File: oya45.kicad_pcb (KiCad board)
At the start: 2 copper layers, 94 parts, among them U1 Elite-C

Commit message: diodes lined up
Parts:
- moved U1 295.5 mm to (213.9, -7.87)
- moved D25 192.2 mm to (-50.2, 37.5), turned to 90 degrees
- moved D22 187.4 mm to (-58.3, 37.5), turned to 90 degrees
- moved D19 182.8 mm to (-62.4, 37.5), turned to 90 degrees
- moved D18 180.3 mm to (-64.4, 37.5), turned to 90 degrees
- moved D17 177.8 mm to (-66.4, 37.5), turned to 90 degrees
- moved D16 175.3 mm to (-68.5, 37.5), turned to 90 degrees
- moved D15 172.8 mm to (-70.5, 37.5), turned to 90 degrees
- moved D9 159.6 mm to (-82.7, 37.5), turned to 90 degrees
- moved D8 157.3 mm to (-84.7, 37.5), turned to 90 degrees
- moved D7 155.0 mm to (-86.7, 37.5), turned to 90 degrees
- moved D44 151.2 mm to (-11.6, 37.5), turned to 90 degrees
- moved D2 146.4 mm to (-96.9, 37.5), turned to 90 degrees
- moved D40 142.8 mm to (-19.7, 37.5), turned to 90 degrees
- moved D39 140.5 mm to (-21.7, 37.5), turned to 90 degrees
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
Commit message: less pads
made a basic pcb instead of complex to make it cheaper
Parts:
- moved D23 252.8 mm to (198.5, 42.5)
- moved D21 252.8 mm to (196.5, 42.5)
- moved D1 252.7 mm to (153.8, 42.5)
- moved D12 252.7 mm to (176.1, 42.5)
- moved D17 252.7 mm to (186.3, 42.5)
- moved D20 252.7 mm to (192.4, 42.5)
- moved D4 252.7 mm to (159.9, 42.5)
- moved D9 252.7 mm to (170.0, 42.5)
- moved D11 252.7 mm to (174.1, 42.5)
- moved D13 252.7 mm to (178.1, 42.5)
- moved D14 252.7 mm to (180.2, 42.5)
- moved D16 252.7 mm to (184.2, 42.5)
- moved D19 252.7 mm to (190.3, 42.5)
- moved D22 252.7 mm to (194.4, 42.5)
- moved D3 252.7 mm to (157.8, 42.5)
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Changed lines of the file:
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@@
   )
   (module Keebio-Parts:Diode-Hybrid-Back (layer B.Cu)
-    (at -9.525 37.465 90)
+    (at 196.50075 32.54375 90)
     (attr smd)
     (fp_text reference D45 (at -0.0254 -1.4 90) (layer F.SilkS)
@@
   )
   (module Keebio-Parts:Diode-Hybrid-Back (layer B.Cu)
-    (at -11.557 37.465 90)
+    (at 194.46875 32.54375 90)
     (attr smd)
     (fp_text reference D44 (at -0.0254 -1.4 90) (layer F.SilkS)
@@
   )
   (module Keebio-Parts:Diode-Hybrid-Back (layer B.Cu)
-    (at -13.589 37.465 90)
+    (at 192.43675 32.54375 90)
     (attr smd)
     (fp_text reference D43 (at -0.0254 -1.4 90) (layer F.SilkS)
@@
   )
   (module Keebio-Parts:Diode-Hybrid-Back (layer B.Cu)
-    (at -15.621 37.465 90)
+    (at 190.40475 32.54375 90)
     (attr smd)
     (fp_text reference D42 (at -0.0254 -1.4 90) (layer F.SilkS)
@@
   )
   (module Keebio-Parts:Diode-Hybrid-Back (layer B.Cu)
-    (at -17.653 37.465 90)
+    (at 188.37275 32.54375 90)
     (attr smd)
     (fp_text reference D41 (at -0.0254 -1.4 90) (layer F.SilkS)
@@
   )
   (module Keebio-Parts:Diode-Hybrid-Back (layer B.Cu)
-    (at -19.685 37.465 90)
+    (at 186.34075 32.54375 90)
     (attr smd)
     (fp_text reference D40 (at -0.0254 -1.4 90) (layer F.SilkS)
@@
   )
   (module Keebio-Parts:Diode-Hybrid-Back (layer B.Cu)
-    (at -21.717 37.465 90)
+    (at 184.30875 32.54375 90)
     (attr smd)
     (fp_text reference D39 (at -0.0254 -1.4 90) (layer F.SilkS)
@@
   )
   (module Keebio-Parts:Diode-Hybrid-Back (layer B.Cu)
-    (at -23.749 37.465 90)
+    (at 182.27675 32.54375 90)
     (attr smd)
     (fp_text reference D38 (at -0.0254 -1.4 90) (layer F.SilkS)
@@
   )
   (module Keebio-Parts:Diode-Hybrid-Back (layer B.Cu)
-    (at -25.781 37.465 90)
+    (at 180.24475 32.54375 90)
     (attr smd)
     (fp_text reference D37 (at -0.0254 -1.4 90) (layer F.SilkS)
@@
   )
   (module Keebio-Parts:Diode-Hybrid-Back (layer B.Cu)
-    (at -27.813 37.465 90)
+    (at 178.21275 32.54375 90)
     (attr smd)
     (fp_text reference D36 (at -0.0254 -1.4 90) (layer F.SilkS)
@@
   )
   (module Keebio-Parts:Diode-Hybrid-Back (layer B.Cu)
-    (at -29.845 37.465 90)
+    (at 176.18075 32.54375 90)
     (attr smd)
     (fp_text reference D35 (at -0.0254 -1.4 90) (layer F.SilkS)
@@
   )
   (module Keebio-Parts:Diode-Hybrid-Back (layer B.Cu)
-    (at -31.877 37.465 90)
+    (at 174.14875 32.54375 90)
     (attr smd)
     (fp_text reference D34 (at -0.0254 -1.4 90) (layer F.SilkS)
@@
   )
   (module Keebio-Parts:Diode-Hybrid-Back (layer B.Cu)
-    (at -33.909 37.465 90)
+    (at 172.11675 32.54375 90)
     (attr smd)
     (fp_text reference D33 (at -0.0254 -1.4 90) (layer F.SilkS)
@@
   )
   (module Keebio-Parts:Diode-Hybrid-Back (layer B.Cu)
-    (at -35.941 37.465 90)
+    (at 170.08475 32.54375 90)
     (attr smd)
     (fp_text reference D32 (at -0.0254 -1.4 90) (layer F.SilkS)
@@
   )
   (module Keebio-Parts:Diode-Hybrid-Back (layer B.Cu)
-    (at -37.973 37.465 90)
+    (at 168.05275 32.54375 90)
     (attr smd)
     (fp_text reference D31 (at -0.0254 -1.4 90) (layer F.SilkS)
@@
   )
   (module Keebio-Parts:Diode-Hybrid-Back (layer B.Cu)
-    (at -40.005 37.465 90)
+    (at 166.02075 32.54375 90)
     (attr smd)
     (fp_text reference D30 (at -0.0254 -1.4 90) (layer F.SilkS)
@@
   )
   (module Keebio-Parts:Diode-Hybrid-Back (layer B.Cu)
-    (at -42.037 37.465 90)
+    (at 163.98875 32.54375 90)
     (attr smd)
     (fp_text reference D29 (at -0.0254 -1.4 90) (layer F.SilkS)
@@
   )
   (module Keebio-Parts:Diode-Hybrid-Back (layer B.Cu)
-    (at -44.069 37.465 90)
+    (at 161.95675 32.54375 90)
     (attr smd)
     (fp_text reference D28 (at -0.0254 -1.4 90) (layer F.SilkS)
@@
   )
   (module Keebio-Parts:Diode-Hybrid-Back (layer B.Cu)
-    (at -46.101 37.465 90)
+    (at 159.92475 32.54375 90)
     (attr smd)
     (fp_text reference D27 (at -0.0254 -1.4 90) (layer F.SilkS)
@@
   )
   (module Keebio-Parts:Diode-Hybrid-Back (layer B.Cu)
-    (at -48.133 37.465 90)
+    (at 157.89275 32.54375 90)
     (attr smd)
     (fp_text reference D26 (at -0.0254 -1.4 90) (layer F.SilkS)
@@
   )
   (module Keebio-Parts:Diode-Hybrid-Back (layer B.Cu)
-    (at -50.165 37.465 90)
+    (at 155.86075 32.54375 90)
     (attr smd)
     (fp_text reference D25 (at -0.0254 -1.4 90) (layer F.SilkS)
@@
   )
   (module Keebio-Parts:Diode-Hybrid-Back (layer B.Cu)
-    (at -52.197 37.465 90)
+    (at 153.82875 32.54375 90)
     (attr smd)
     (fp_text reference D24 (at -0.0254 -1.4 90) (layer F.SilkS)
@@
   )
   (module Keebio-Parts:Diode-Hybrid-Back (layer B.Cu)
-    (at -54.229 37.465 90)
+    (at 198.501 42.545 90)
     (attr smd)
     (fp_text reference D23 (at -0.0254 -1.4 90) (layer F.SilkS)
@@
   )
   (module Keebio-Parts:Diode-Hybrid-Back (layer B.Cu)
-    (at -58.293 37.465 90)
+    (at 194.40525 42.545 90)
     (attr smd)
     (fp_text reference D22 (at -0.0254 -1.4 90) (layer F.SilkS)
@@
   )
   (module Keebio-Parts:Diode-Hybrid-Back (layer B.Cu)
-    (at -56.261 37.465 90)
+    (at 196.469 42.545 90)
     (attr smd)
     (fp_text reference D21 (at -0.0254 -1.4 90) (layer F.SilkS)
@@
   )
   (module Keebio-Parts:Diode-Hybrid-Back (layer B.Cu)
-    (at -60.325 37.465 90)
+    (at 192.37325 42.545 90)
     (attr smd)
     (fp_text reference D20 (at -0.0254 -1.4 90) (layer F.SilkS)
@@
   )
   (module Keebio-Parts:Diode-Hybrid-Back (layer B.Cu)
-    (at -62.357 37.465 90)
+    (at 190.34125 42.545 90)
     (attr smd)
     (fp_text reference D19 (at -0.0254 -1.4 90) (layer F.SilkS)
@@
   )
   (module Keebio-Parts:Diode-Hybrid-Back (layer B.Cu)
-    (at -64.389 37.465 90)
+    (at 188.30925 42.545 90)
     (attr smd)
     (fp_text reference D18 (at -0.0254 -1.4 90) (layer F.SilkS)
@@
   )
   (module Keebio-Parts:Diode-Hybrid-Back (layer B.Cu)
-    (at -66.421 37.465 90)
+    (at 186.27725 42.545 90)
     (attr smd)
     (fp_text reference D17 (at -0.0254 -1.4 90) (layer F.SilkS)
@@
   )
   (module Keebio-Parts:Diode-Hybrid-Back (layer B.Cu)
-    (at -68.453 37.465 90)
+    (at 184.24525 42.545 90)
     (attr smd)
     (fp_text reference D16 (at -0.0254 -1.4 90) (layer F.SilkS)
@@
   )
   (module Keebio-Parts:Diode-Hybrid-Back (layer B.Cu)
-    (at -70.485 37.465 90)
+    (at 182.21325 42.545 90)
     (attr smd)
     (fp_text reference D15 (at -0.0254 -1.4 90) (layer F.SilkS)
@@
   )
   (module Keebio-Parts:Diode-Hybrid-Back (layer B.Cu)
-    (at -72.517 37.465 90)
+    (at 180.18125 42.545 90)
     (attr smd)
     (fp_text reference D14 (at -0.0254 -1.4 90) (layer F.SilkS)
@@
   )
   (module Keebio-Parts:Diode-Hybrid-Back (layer B.Cu)
-    (at -74.549 37.465 90)
+    (at 178.14925 42.545 90)
     (attr smd)
     (fp_text reference D13 (at -0.0254 -1.4 90) (layer F.SilkS)
@@
   )
   (module Keebio-Parts:Diode-Hybrid-Back (layer B.Cu)
-    (at -76.581 37.465 90)
+    (at 176.11725 42.545 90)
     (attr smd)
     (fp_text reference D12 (at -0.0254 -1.4 90) (layer F.SilkS)
@@
   )
   (module Keebio-Parts:Diode-Hybrid-Back (layer B.Cu)
-    (at -78.613 37.465 90)
+    (at 174.08525 42.545 90)
     (attr smd)
     (fp_text reference D11 (at -0.0254 -1.4 90) (layer F.SilkS)
@@
   )
   (module Keebio-Parts:Diode-Hybrid-Back (layer B.Cu)
-    (at -80.645 37.465 90)
+    (at 172.05325 42.545 90)
     (attr smd)
     (fp_text reference D10 (at -0.0254 -1.4 90) (layer F.SilkS)
@@
   )
   (module Keebio-Parts:Diode-Hybrid-Back (layer B.Cu)
-    (at -82.677 37.465 90)
+    (at 170.02125 42.545 90)
     (attr smd)
     (fp_text reference D9 (at -0.0254 -1.4 90) (layer F.SilkS)
@@
   )
   (module Keebio-Parts:Diode-Hybrid-Back (layer B.Cu)
-    (at -84.709 37.465 90)
+    (at 167.98925 42.545 90)
     (attr smd)
     (fp_text reference D8 (at -0.0254 -1.4 90) (layer F.SilkS)
@@
   )
   (module Keebio-Parts:Diode-Hybrid-Back (layer B.Cu)
-    (at -86.741 37.465 90)
+    (at 165.95725 42.545 90)
     (attr smd)
     (fp_text reference D7 (at -0.0254 -1.4 90) (layer F.SilkS)
@@
   )
   (module Keebio-Parts:Diode-Hybrid-Back (layer B.Cu)
-    (at -88.773 37.465 90)
+    (at 163.92525 42.545 90)
     (attr smd)
     (fp_text reference D6 (at -0.0254 -1.4 90) (layer F.SilkS)
@@
   )
   (module Keebio-Parts:Diode-Hybrid-Back (layer B.Cu)
-    (at -90.805 37.465 90)
+    (at 161.89325 42.545 90)
     (attr smd)
     (fp_text reference D5 (at -0.0254 -1.4 90) (layer F.SilkS)
@@
   )
   (module Keebio-Parts:Diode-Hybrid-Back (layer B.Cu)
-    (at -92.837 37.465 90)
+    (at 159.86125 42.545 90)
     (attr smd)
     (fp_text reference D4 (at -0.0254 -1.4 90) (layer F.SilkS)
@@
   )
   (module Keebio-Parts:Diode-Hybrid-Back (layer B.Cu)
-    (at -94.869 37.465 90)
+    (at 157.82925 42.545 90)
     (attr smd)
     (fp_text reference D3 (at -0.0254 -1.4 90) (layer F.SilkS)
@@
   )
   (module Keebio-Parts:Diode-Hybrid-Back (layer B.Cu)
-    (at -96.901 37.465 90)
+    (at 155.79725 42.545 90)
     (attr smd)
     (fp_text reference D2 (at -0.0254 -1.4 90) (layer F.SilkS)
@@
   )
   (module Keebio-Parts:Diode-Hybrid-Back (layer B.Cu)
-    (at -98.933 37.465 90)
+    (at 153.76525 42.545 90)
     (attr smd)
     (fp_text reference D1 (at -0.0254 -1.4 90) (layer F.SilkS)

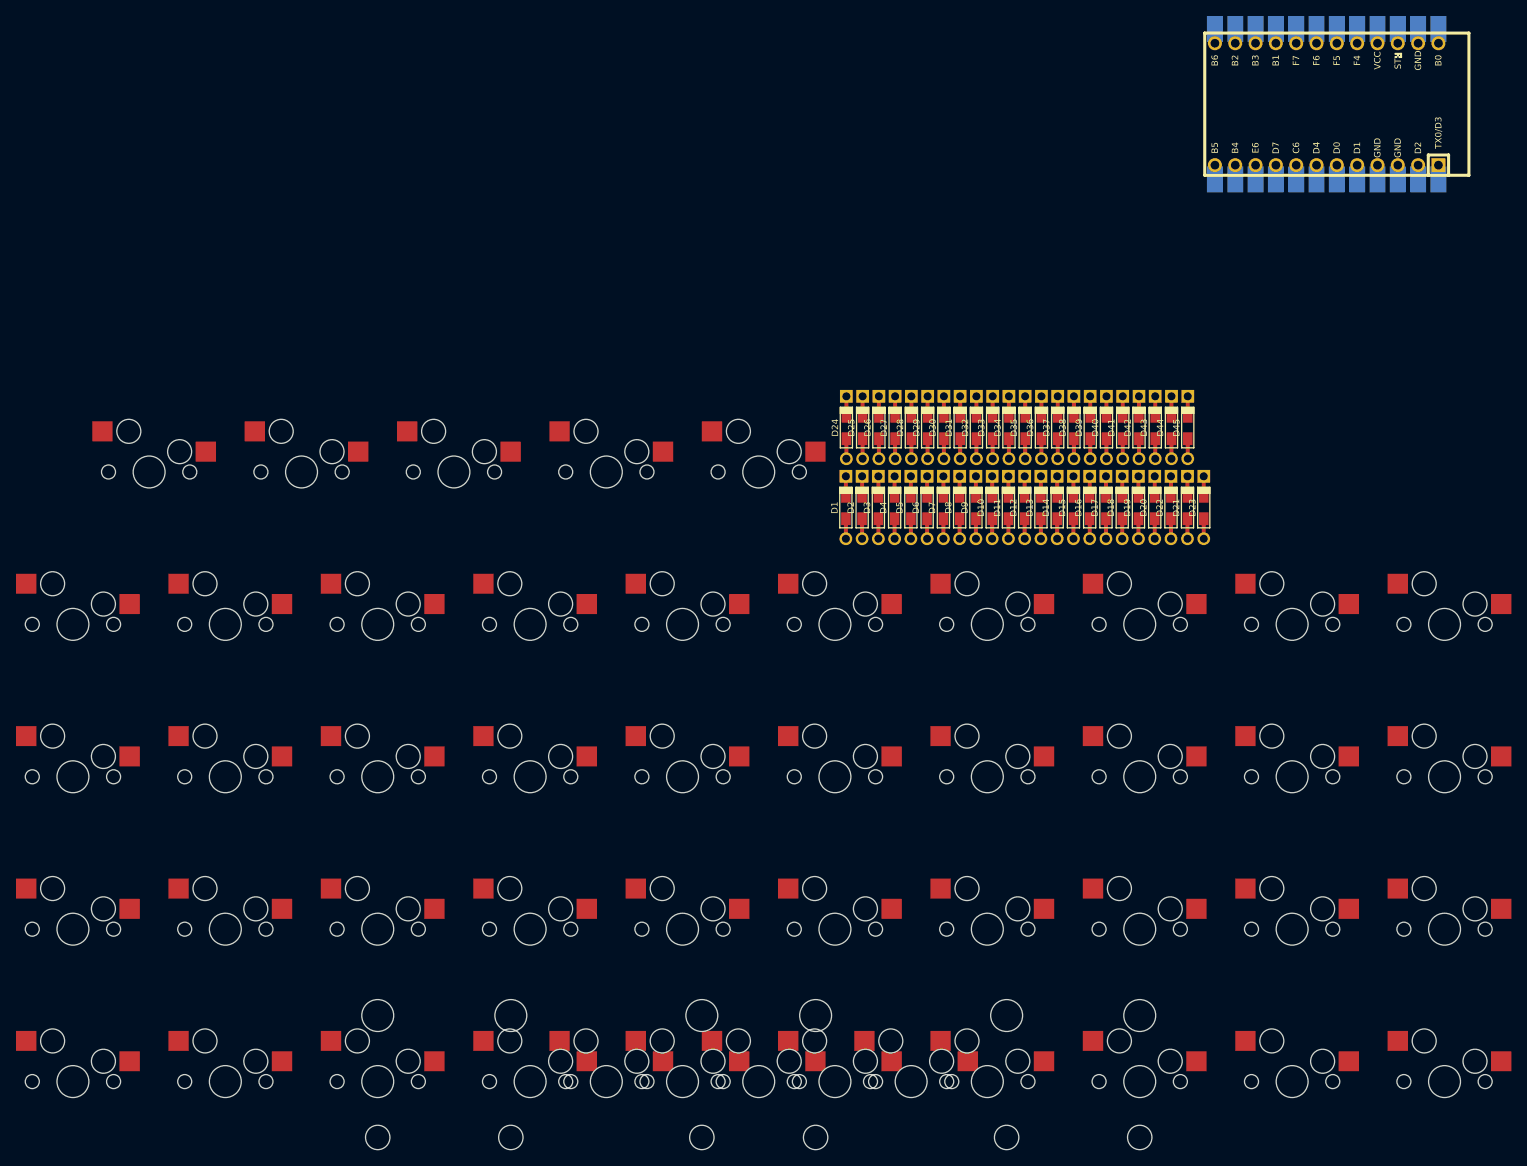
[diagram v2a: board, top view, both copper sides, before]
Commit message: diodes finished
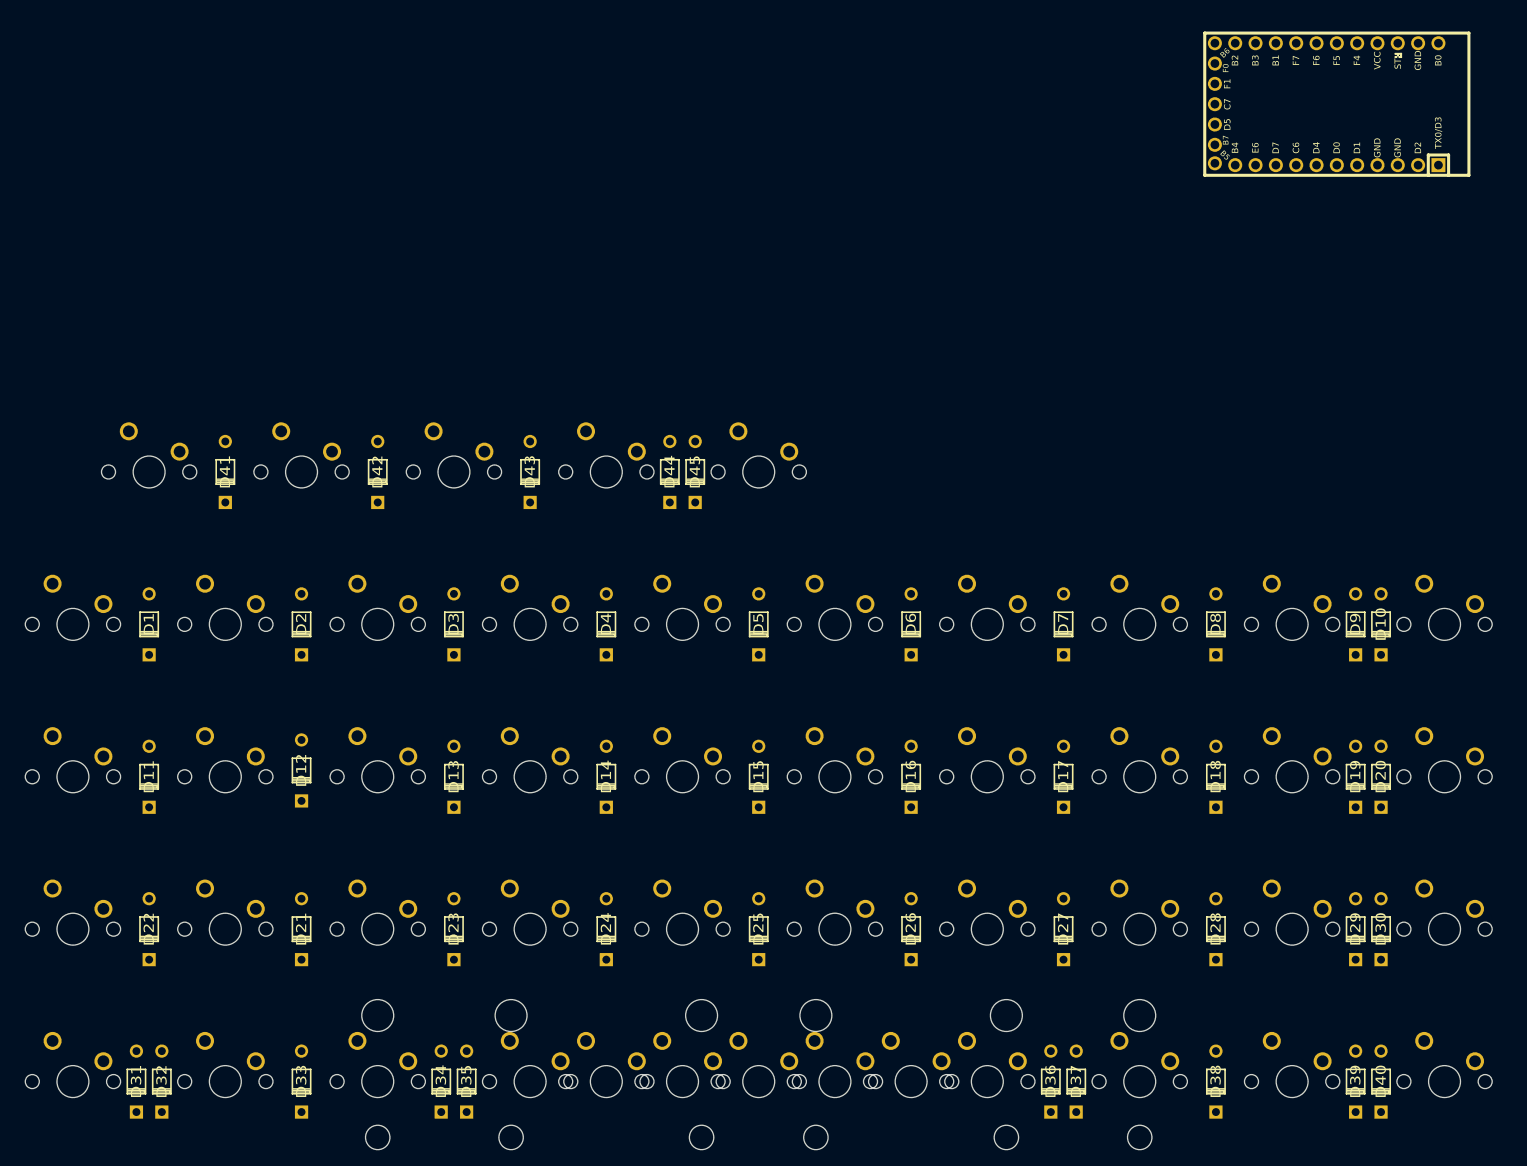
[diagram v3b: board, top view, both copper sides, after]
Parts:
- D1, D10, D11, D12, D13, D14, D15, D16, D17, D18, D19, D2, D20, D21, D22, D23, D24, D25, D26, D27, D28, D29, D3, D30, D31, D32, D33, D34, D35, D36, D37, D38, D39, D4, D40, D41, D42, D43, D44, D45, D5, D6, D7, D8, D9: footprint Keebio-Parts:Diode-Hybrid-Back -> Keebio-Parts:Diode; moved to F.Cu
- MX1, MX10, MX11, MX12, MX13, MX14, MX15, MX16, MX17, MX18, MX19, MX2, MX20, MX21, MX22, MX23, MX24, MX25, MX26, MX27, MX28, MX29, MX3, MX30, MX31, MX32, MX33, MX34, MX35, MX36, MX37, MX38, MX39, MX4, MX40, MX41, MX42, MX43, MX44, MX45, MX5, MX6, MX7, MX8, MX9: footprint MX_Only:MXOnly-1U-Hotswap -> MX_Only:MXOnly-1U-NoLED
- MX46: footprint MX_Only:MXOnly-6U-Centered-Hotswap-ReversedStabilizers -> MX_Only:MXOnly-6U-Centered-ReversedStabilizers-NoLED
- MX47, MX48: footprint MX_Only:MXOnly-2U-Hotswap-ReversedStabilizers -> MX_Only:MXOnly-2U-ReversedStabilizers-NoLED
- U1: footprint Keebio-Parts:Elite-C-castellated-24pin-holes -> Keebio-Parts:Elite-C
- moved D22 138.2 mm to (66.7, 95.2), turned to 270 degrees
- moved D31 131.5 mm to (65.1, 114.3), turned to 270 degrees
- moved D32 130.6 mm to (68.3, 114.3), turned to 270 degrees
- moved D21 122.6 mm to (85.7, 95.2), turned to 270 degrees
- moved D33 118.9 mm to (85.7, 114.3), turned to 270 degrees
- moved D11 112.6 mm to (66.7, 76.2), turned to 270 degrees
- moved D41 112.3 mm to (76.2, 38.1), turned to 270 degrees
- moved D34 108.3 mm to (103.2, 114.3), turned to 270 degrees
- moved D23 107.5 mm to (104.8, 95.2), turned to 270 degrees
- moved D35 107.5 mm to (106.4, 114.3), turned to 270 degrees
- moved D12 96.2 mm to (85.7, 75.4), turned to 270 degrees
- moved D42 95.3 mm to (95.2, 38.1), turned to 270 degrees
- moved D40 88.7 mm to (220.7, 114.3), turned to 270 degrees
- moved D1 88.3 mm to (66.7, 57.1), turned to 270 degrees
- moved D39 88.2 mm to (217.5, 114.3), turned to 270 degrees
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
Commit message: save
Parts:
- U1: moved to F.Cu
- moved U1 46.4 mm to (219.9, 38.1)
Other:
- net class Default: clearance 0.2 -> 0.00508; trace_width 0.25 -> 0.00508
- rule trace_clearance: 0.2 -> 0.00508
- rule trace_min: 0.2 -> 0.00381
- rule via_min_drill: 0.3 -> 0.00762
- rule via_min_size: 0.4 -> 0.00381
